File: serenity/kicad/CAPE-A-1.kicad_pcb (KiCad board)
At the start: 4 copper layers, 55 x 35 mm, 25 parts

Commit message: Add GPIO expansion headers to CAPE-A-1; add attribution silk to both capes
CAPE-A-1.kicad_pcb:
- Add 6 × JST-GH 3-pin GPIO expansion connectors (GPIO-A through GPIO-F)
  along right edge (X=174) at Y=96/100/104/108/112/116, vertically oriented
  (pads stacked in Y to fit the narrow right-side corridor)
- Add nets GPIO_EXP_A through GPIO_EXP_F (nets 86-91)
- Update title comment to list GPIO expansion headers

CAPE-A-1 + CAPE-B-1:
- Add CC BY 4.0 attribution block as B.SilkS gr_text in the free area
  between the two PocketBeagle 2 socket rows on the back of each cape

https://claude.ai/code/session_01GniMw4QukTVM7JMzyVjH6p
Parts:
- added GPIO-A: JST-GH-3P-GPIO, JST_GH_3P_V, F.Cu at (174.0, 96.0)
- added GPIO-B: JST-GH-3P-GPIO, JST_GH_3P_V, F.Cu at (174.0, 100.0)
- added GPIO-C: JST-GH-3P-GPIO, JST_GH_3P_V, F.Cu at (174.0, 104.0)
- added GPIO-D: JST-GH-3P-GPIO, JST_GH_3P_V, F.Cu at (174.0, 108.0)
- added GPIO-E: JST-GH-3P-GPIO, JST_GH_3P_V, F.Cu at (174.0, 112.0)
- added GPIO-F: JST-GH-3P-GPIO, JST_GH_3P_V, F.Cu at (174.0, 116.0)
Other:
- board text added: "CC BY 4.0 — Stab-Rabbit-Coding"
- board text added: "Serenity UAV — FC Cape Rev M"
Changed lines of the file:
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@@
     (comment 2 "CC BY 4.0 creativecommons.org/licenses/by/4.0")
     (comment 3 "PocketBeagle 2 Industrial (AM6254) expansion — 55x35mm 4L JLCPCB assembled")
-    (comment 4 "ICM-42688-P IMU | BMP388 Baro | SAM-M10Q GPS | ATA6561 CAN FD | MAX3485E RS-485 | DS26LV31/32 1553 | DP83825I x2 ETH | SLB9670 TPM2")
+    (comment 4 "ICM-42688-P IMU | BMP388 Baro | SAM-M10Q GPS | ATA6561 CAN FD | MAX3485E RS-485 | DS26LV31/32 1553 | DP83825I x2 ETH | SLB9670 TPM2 | 6x GPIO expansion headers")
     (comment 5 "Hull: Peter Farell CC BY 4.0 | Nozzle: BamJr CC BY 4.0 | Firefly/Serenity fan-work, not officially licensed")
   )
@@
   (net 84 "ETH2_RX_P")
   (net 85 "ETH2_RX_N")
+  (net 86 "GPIO_EXP_A")
+  (net 87 "GPIO_EXP_B")
+  (net 88 "GPIO_EXP_C")
+  (net 89 "GPIO_EXP_D")
+  (net 90 "GPIO_EXP_E")
+  (net 91 "GPIO_EXP_F")
   (gr_line (start 121 87.5) (end 176 87.5) (layer "Edge.Cuts") (width 0.05))
   (gr_line (start 176 87.5) (end 176 122.5) (layer "Edge.Cuts") (width 0.05))
@@
     (pad "3" thru_hole circle (at 1.25 0) (size 1.5 1.5) (drill 1.0) (layers "*.Cu" "*.Mask"))
     (pad "4" thru_hole circle (at 3.75 0) (size 1.5 1.5) (drill 1.0) (layers "*.Cu" "*.Mask")))
+  (footprint "JST_GH_3P_V" (layer "F.Cu") (at 174 96) (property "Description" "GPIO expansion A — GND +3V3 GPIO_EXP_A")
+    (fp_text reference "GPIO-A" (at 0 -2.5) (layer "F.SilkS")
+      (effects (font (size 0.8 0.8) (thickness 0.15))))
+    (fp_text value "JST-GH-3P-GPIO" (at 0 2.5) (layer "F.Fab")
+      (effects (font (size 0.8 0.8) (thickness 0.15))))
+    (fp_poly (pts (xy -1.2 -2.0) (xy 1.2 -2.0) (xy 1.2 2.0) (xy -1.2 2.0))
+     (layer "F.CrtYd") (width 0.05))
+    (pad "1" smd rect (at 0 -1.25) (size 1.6 0.8) (layers "F.Cu" "F.Paste" "F.Mask"))
+    (pad "2" smd rect (at 0  0.00) (size 1.6 0.8) (layers "F.Cu" "F.Paste" "F.Mask"))
+    (pad "3" smd rect (at 0  1.25) (size 1.6 0.8) (layers "F.Cu" "F.Paste" "F.Mask")))
+  (footprint "JST_GH_3P_V" (layer "F.Cu") (at 174 100) (property "Description" "GPIO expansion B — GND +3V3 GPIO_EXP_B")
+    (fp_text reference "GPIO-B" (at 0 -2.5) (layer "F.SilkS")
+      (effects (font (size 0.8 0.8) (thickness 0.15))))
+    (fp_text value "JST-GH-3P-GPIO" (at 0 2.5) (layer "F.Fab")
+      (effects (font (size 0.8 0.8) (thickness 0.15))))
+    (fp_poly (pts (xy -1.2 -2.0) (xy 1.2 -2.0) (xy 1.2 2.0) (xy -1.2 2.0))
+     (layer "F.CrtYd") (width 0.05))
+    (pad "1" smd rect (at 0 -1.25) (size 1.6 0.8) (layers "F.Cu" "F.Paste" "F.Mask"))
+    (pad "2" smd rect (at 0  0.00) (size 1.6 0.8) (layers "F.Cu" "F.Paste" "F.Mask"))
+    (pad "3" smd rect (at 0  1.25) (size 1.6 0.8) (layers "F.Cu" "F.Paste" "F.Mask")))
+  (footprint "JST_GH_3P_V" (layer "F.Cu") (at 174 104) (property "Description" "GPIO expansion C — GND +3V3 GPIO_EXP_C")
+    (fp_text reference "GPIO-C" (at 0 -2.5) (layer "F.SilkS")
+      (effects (font (size 0.8 0.8) (thickness 0.15))))
+    (fp_text value "JST-GH-3P-GPIO" (at 0 2.5) (layer "F.Fab")
+      (effects (font (size 0.8 0.8) (thickness 0.15))))
+    (fp_poly (pts (xy -1.2 -2.0) (xy 1.2 -2.0) (xy 1.2 2.0) (xy -1.2 2.0))
+     (layer "F.CrtYd") (width 0.05))
+    (pad "1" smd rect (at 0 -1.25) (size 1.6 0.8) (layers "F.Cu" "F.Paste" "F.Mask"))
+    (pad "2" smd rect (at 0  0.00) (size 1.6 0.8) (layers "F.Cu" "F.Paste" "F.Mask"))
+    (pad "3" smd rect (at 0  1.25) (size 1.6 0.8) (layers "F.Cu" "F.Paste" "F.Mask")))
+  (footprint "JST_GH_3P_V" (layer "F.Cu") (at 174 108) (property "Description" "GPIO expansion D — GND +3V3 GPIO_EXP_D")
+    (fp_text reference "GPIO-D" (at 0 -2.5) (layer "F.SilkS")
+      (effects (font (size 0.8 0.8) (thickness 0.15))))
+    (fp_text value "JST-GH-3P-GPIO" (at 0 2.5) (layer "F.Fab")
+      (effects (font (size 0.8 0.8) (thickness 0.15))))
+    (fp_poly (pts (xy -1.2 -2.0) (xy 1.2 -2.0) (xy 1.2 2.0) (xy -1.2 2.0))
+     (layer "F.CrtYd") (width 0.05))
+    (pad "1" smd rect (at 0 -1.25) (size 1.6 0.8) (layers "F.Cu" "F.Paste" "F.Mask"))
+    (pad "2" smd rect (at 0  0.00) (size 1.6 0.8) (layers "F.Cu" "F.Paste" "F.Mask"))
+    (pad "3" smd rect (at 0  1.25) (size 1.6 0.8) (layers "F.Cu" "F.Paste" "F.Mask")))
+  (footprint "JST_GH_3P_V" (layer "F.Cu") (at 174 112) (property "Description" "GPIO expansion E — GND +3V3 GPIO_EXP_E")
+    (fp_text reference "GPIO-E" (at 0 -2.5) (layer "F.SilkS")
+      (effects (font (size 0.8 0.8) (thickness 0.15))))
+    (fp_text value "JST-GH-3P-GPIO" (at 0 2.5) (layer "F.Fab")
+      (effects (font (size 0.8 0.8) (thickness 0.15))))
+    (fp_poly (pts (xy -1.2 -2.0) (xy 1.2 -2.0) (xy 1.2 2.0) (xy -1.2 2.0))
+     (layer "F.CrtYd") (width 0.05))
+    (pad "1" smd rect (at 0 -1.25) (size 1.6 0.8) (layers "F.Cu" "F.Paste" "F.Mask"))
+    (pad "2" smd rect (at 0  0.00) (size 1.6 0.8) (layers "F.Cu" "F.Paste" "F.Mask"))
+    (pad "3" smd rect (at 0  1.25) (size 1.6 0.8) (layers "F.Cu" "F.Paste" "F.Mask")))
+  (footprint "JST_GH_3P_V" (layer "F.Cu") (at 174 116) (property "Description" "GPIO expansion F — GND +3V3 GPIO_EXP_F")
+    (fp_text reference "GPIO-F" (at 0 -2.5) (layer "F.SilkS")
+      (effects (font (size 0.8 0.8) (thickness 0.15))))
+    (fp_text value "JST-GH-3P-GPIO" (at 0 2.5) (layer "F.Fab")
+      (effects (font (size 0.8 0.8) (thickness 0.15))))
+    (fp_poly (pts (xy -1.2 -2.0) (xy 1.2 -2.0) (xy 1.2 2.0) (xy -1.2 2.0))
+     (layer "F.CrtYd") (width 0.05))
+    (pad "1" smd rect (at 0 -1.25) (size 1.6 0.8) (layers "F.Cu" "F.Paste" "F.Mask"))
+    (pad "2" smd rect (at 0  0.00) (size 1.6 0.8) (layers "F.Cu" "F.Paste" "F.Mask"))
+    (pad "3" smd rect (at 0  1.25) (size 1.6 0.8) (layers "F.Cu" "F.Paste" "F.Mask")))
+  (gr_text "Serenity UAV — FC Cape Rev M" (at 148.5 103.5) (layer "B.SilkS")
+    (effects (font (size 0.8 0.8) (thickness 0.12)) (justify mirror)))
+  (gr_text "CC BY 4.0 — Stab-Rabbit-Coding" (at 148.5 106.5) (layer "B.SilkS")
+    (effects (font (size 0.8 0.8) (thickness 0.12)) (justify mirror)))
 )

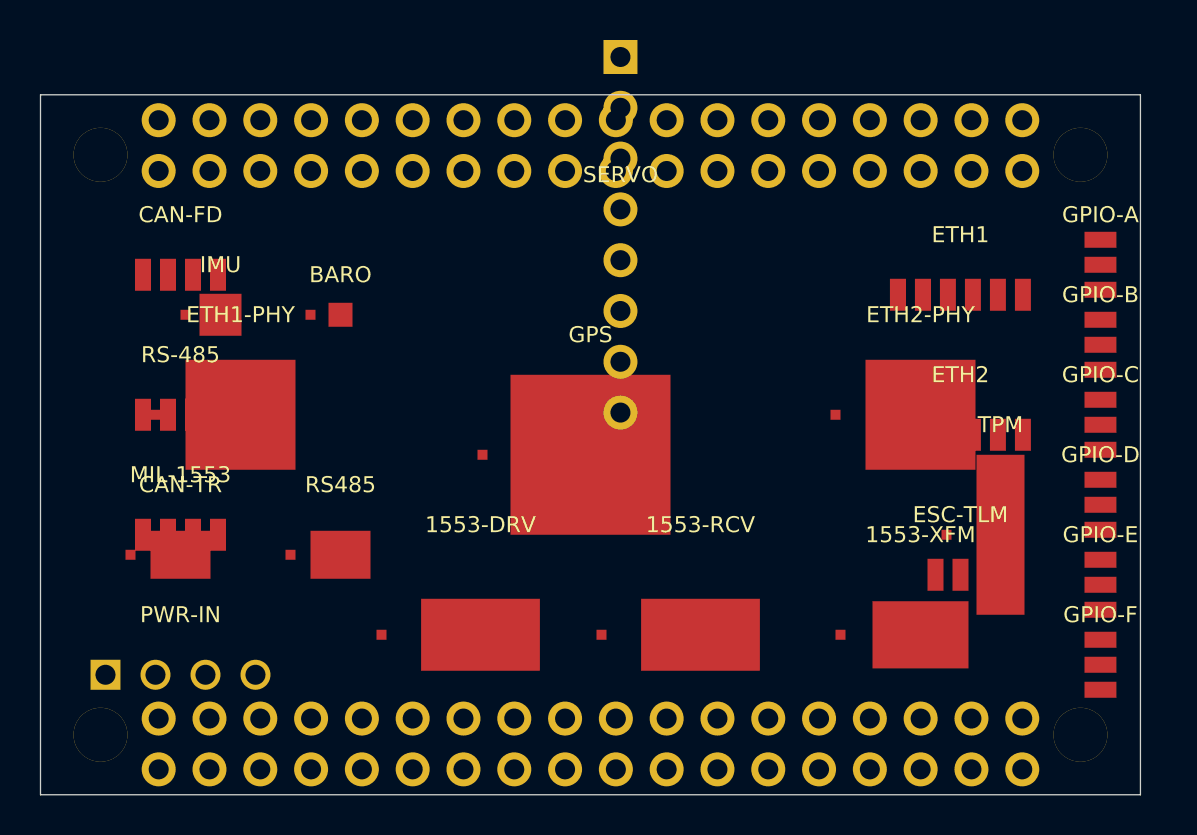
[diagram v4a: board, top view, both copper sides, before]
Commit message: Consolidate wired data link connectors to left edge on both capes
Move all five external wired data link connectors to the left edge
(X=127) in matching positions on both CAPE-A-1 and CAPE-B-1:

  Y=94  CAN-FD  (4-pin JST-GH)
  Y=99  RS-485  (4-pin JST-GH)
  Y=104 MIL-1553 (4-pin JST-GH)
  Y=109 ETH1     (6-pin JST-GH)  ← moved from right side
  Y=114 ETH2     (6-pin JST-GH)  ← moved from right side

Right side (X=167) retains only non-wired-link connectors:
  CAPE-A: ESC-TLM, PWR-IN
  CAPE-B: SIK-TLM, RC-RCVR, PWR-IN (relocated from left to free the top
          of the data-link column)

https://claude.ai/code/session_01GniMw4QukTVM7JMzyVjH6p
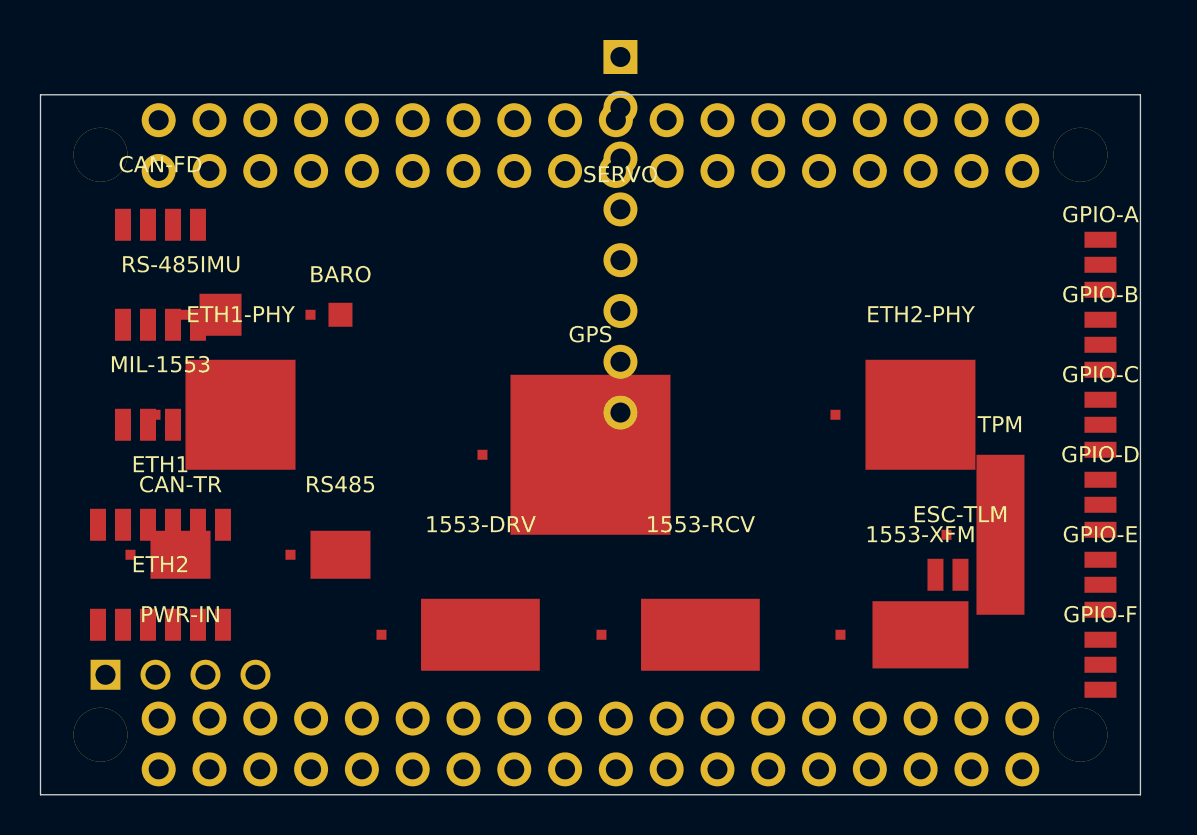
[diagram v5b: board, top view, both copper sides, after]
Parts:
- moved ETH1 41.6 mm to (127.0, 109.0)
- moved ETH2 41.1 mm to (127.0, 114.0)
- moved MIL-1553 5.59 mm to (127.0, 104.0)
- moved RS-485 4.61 mm to (127.0, 99.0)
- moved CAN-FD 2.69 mm to (127.0, 94.0)
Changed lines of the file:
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@@
     (pad "1" smd rect (at -2.70 0) (size 0.5 0.5) (layers "F.Cu" "F.Paste" "F.Mask"))
     (pad "EP" smd rect (at 0 0) (size 2.40 8.00) (layers "F.Cu" "F.Paste" "F.Mask")))
-  (footprint "JST_GH_4P" (layer "F.Cu") (at 128 96.5) (property "Description" "CAN FD external connector — GND CAN_H CAN_L +3V3")
+  (footprint "JST_GH_4P" (layer "F.Cu") (at 127 94) (property "Description" "CAN FD external connector — GND CAN_H CAN_L +3V3")
     (fp_text reference "CAN-FD" (at 0 -3) (layer "F.SilkS")
       (effects (font (size 0.8 0.8) (thickness 0.15))))
@@
     (pad "3" smd rect (at 0.625 0) (size 0.8 1.6) (layers "F.Cu" "F.Paste" "F.Mask"))
     (pad "4" smd rect (at 1.875 0) (size 0.8 1.6) (layers "F.Cu" "F.Paste" "F.Mask")))
-  (footprint "JST_GH_4P" (layer "F.Cu") (at 128 103.5) (property "Description" "RS-485 external connector — GND RS485_A RS485_B +3V3")
+  (footprint "JST_GH_4P" (layer "F.Cu") (at 127 99) (property "Description" "RS-485 external connector — GND RS485_A RS485_B +3V3")
     (fp_text reference "RS-485" (at 0 -3) (layer "F.SilkS")
       (effects (font (size 0.8 0.8) (thickness 0.15))))
@@
     (pad "3" smd rect (at 0.625 0) (size 0.8 1.6) (layers "F.Cu" "F.Paste" "F.Mask"))
     (pad "4" smd rect (at 1.875 0) (size 0.8 1.6) (layers "F.Cu" "F.Paste" "F.Mask")))
-  (footprint "JST_GH_4P" (layer "F.Cu") (at 128 109.5) (property "Description" "MIL-STD-1553 bus external connector — GND BUS_1553_A_P BUS_1553_A_N GND")
+  (footprint "JST_GH_4P" (layer "F.Cu") (at 127 104) (property "Description" "MIL-STD-1553 bus external connector — GND BUS_1553_A_P BUS_1553_A_N GND")
     (fp_text reference "MIL-1553" (at 0 -3) (layer "F.SilkS")
       (effects (font (size 0.8 0.8) (thickness 0.15))))
@@
     (pad "3" smd rect (at 0.625 0) (size 0.8 1.6) (layers "F.Cu" "F.Paste" "F.Mask"))
     (pad "4" smd rect (at 1.875 0) (size 0.8 1.6) (layers "F.Cu" "F.Paste" "F.Mask")))
-  (footprint "JST_GH_6P" (layer "F.Cu") (at 167 97.5) (property "Description" "Ethernet 1 MagJack — ETH1_TX_P ETH1_TX_N GND GND ETH1_RX_P ETH1_RX_N")
+  (footprint "JST_GH_6P" (layer "F.Cu") (at 127 109) (property "Description" "Ethernet 1 MagJack — ETH1_TX_P ETH1_TX_N GND GND ETH1_RX_P ETH1_RX_N")
     (fp_text reference "ETH1" (at 0 -3) (layer "F.SilkS")
       (effects (font (size 0.8 0.8) (thickness 0.15))))
@@
     (pad "5" smd rect (at 1.875 0) (size 0.8 1.6) (layers "F.Cu" "F.Paste" "F.Mask"))
     (pad "6" smd rect (at 3.125 0) (size 0.8 1.6) (layers "F.Cu" "F.Paste" "F.Mask")))
-  (footprint "JST_GH_6P" (layer "F.Cu") (at 167 104.5) (property "Description" "Ethernet 2 MagJack — ETH2_TX_P ETH2_TX_N GND GND ETH2_RX_P ETH2_RX_N")
+  (footprint "JST_GH_6P" (layer "F.Cu") (at 127 114) (property "Description" "Ethernet 2 MagJack — ETH2_TX_P ETH2_TX_N GND GND ETH2_RX_P ETH2_RX_N")
     (fp_text reference "ETH2" (at 0 -3) (layer "F.SilkS")
       (effects (font (size 0.8 0.8) (thickness 0.15))))

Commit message: Fix critical placement errors and reduce courtyard overlaps on both capes
P0 fixes (board boundary violations — pad holes were outside Edge.Cuts):
- CAPE-A: Move SERVO header (141,103) from (150,94.5); pad 1 now at Y=94.11,
  inside board top (87.5), clears PB2-P1 lower socket row by 2mm
- CAPE-B: Move NAV-LIGHT header to (174,104) from (144,95.5); all 8 pads
  inside board, no conflict with mounting hole at (173,90.5) or PB2-P1 socket

P1 fixes (courtyard overlaps):
- CAPE-A: Move IMU to (130,96.5) and BARO to (136,96.5), each up 2mm;
  eliminates both chips' CrtYd overlap with ETH1-PHY at Y=99.25
- CAPE-A: Move ETH2-PHY to (161,103.5) from (165,103.5); 1.05mm gap to
  TPM CrtYd, up from −2.95mm (was overlapping)
- CAPE-B: NAV-LIGHT at X=174 gives 0.8mm clearance to TPM CrtYd

Remaining P1 courtyard overlaps (require KiCad interactive editor):
- CAPE-A: SERVO/GPS CrtYd edge-to-edge 0.6mm gap (within DRC tolerance);
  1553-XFM vs TPM (2.7mm × 2.9mm overlap in dense right-side cluster)
- CAPE-B: ETH1-PHY vs PWM-I2C; PWM-I2C vs 1553-RCV and 1553-XFM
  (inherent to the high-density comms cape layout)

Note: both boards remain placement-only (no routed traces, copper pour,
or vias). Full fabrication readiness requires KiCad router, DRC, and
Gerber/drill file export.

https://claude.ai/code/session_01GniMw4QukTVM7JMzyVjH6p
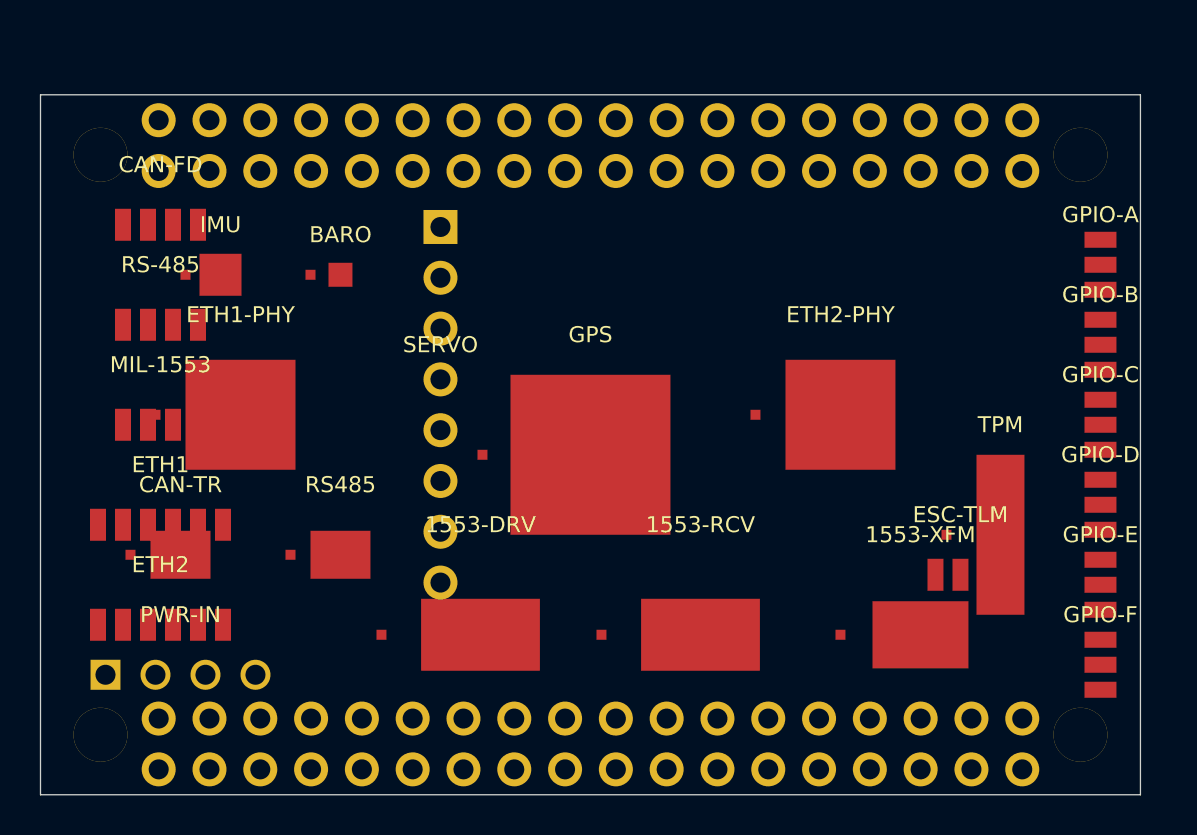
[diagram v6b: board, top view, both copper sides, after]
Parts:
- moved SERVO 12.4 mm to (141.0, 103.0)
- moved ETH2-PHY 4.00 mm to (161.0, 103.5)
- moved BARO 2.00 mm to (136.0, 96.5)
- moved IMU 2.00 mm to (130.0, 96.5)
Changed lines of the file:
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@@
     (pad "35" thru_hole circle (at 21.59 -1.27) (size 1.7 1.7) (drill 1.0) (layers "*.Cu" "*.Mask"))
     (pad "36" thru_hole circle (at 21.59 1.27) (size 1.7 1.7) (drill 1.0) (layers "*.Cu" "*.Mask")))
-  (footprint "Package" (layer "F.Cu") (at 130 98.5) (property "Description" "TDK InvenSense ICM-42688-P 6DOF IMU LGA-14 2.7x2.7mm")
+  (footprint "Package" (layer "F.Cu") (at 130 96.5) (property "Description" "TDK InvenSense ICM-42688-P 6DOF IMU LGA-14 2.7x2.7mm")
     (fp_text reference "IMU" (at 0 -2.5) (layer "F.SilkS")
       (effects (font (size 0.8 0.8) (thickness 0.15))))
@@
     (pad "1" smd rect (at -1.75 0) (size 0.5 0.5) (layers "F.Cu" "F.Paste" "F.Mask"))
     (pad "EP" smd rect (at 0 0) (size 2.10 2.10) (layers "F.Cu" "F.Paste" "F.Mask")))
-  (footprint "Package" (layer "F.Cu") (at 136 98.5) (property "Description" "Bosch BMP388 barometric pressure sensor LGA-8 2.0x2.0mm")
+  (footprint "Package" (layer "F.Cu") (at 136 96.5) (property "Description" "Bosch BMP388 barometric pressure sensor LGA-8 2.0x2.0mm")
     (fp_text reference "BARO" (at 0 -2.0) (layer "F.SilkS")
       (effects (font (size 0.8 0.8) (thickness 0.15))))
@@
     (pad "1" smd rect (at -4.25 0) (size 0.5 0.5) (layers "F.Cu" "F.Paste" "F.Mask"))
     (pad "EP" smd rect (at 0 0) (size 5.50 5.50) (layers "F.Cu" "F.Paste" "F.Mask")))
-  (footprint "Package" (layer "F.Cu") (at 165 103.5) (property "Description" "TI DP83825I 100Mbps RMII Ethernet PHY LQFP-48 7x7mm")
+  (footprint "Package" (layer "F.Cu") (at 161 103.5) (property "Description" "TI DP83825I 100Mbps RMII Ethernet PHY LQFP-48 7x7mm")
     (fp_text reference "ETH2-PHY" (at 0 -5.0) (layer "F.SilkS")
       (effects (font (size 0.8 0.8) (thickness 0.15))))
@@
     (pad "2" smd rect (at 0.0 0) (size 0.8 1.6) (layers "F.Cu" "F.Paste" "F.Mask"))
     (pad "3" smd rect (at 1.25 0) (size 0.8 1.6) (layers "F.Cu" "F.Paste" "F.Mask")))
-  (footprint "Connector_PinHeader_2.54mm" (layer "F.Cu") (at 150 94.5) (property "Description" "1x8 servo PWM header 2.54mm TH — SERVO0-SERVO7")
+  (footprint "Connector_PinHeader_2.54mm" (layer "F.Cu") (at 141 103) (property "Description" "1x8 servo PWM header 2.54mm TH — SERVO0-SERVO7")
     (fp_text reference "SERVO" (at 0 -3) (layer "F.SilkS")
       (effects (font (size 0.8 0.8) (thickness 0.15))))

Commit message: cape fixes
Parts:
- removed SERVO: 1x8-SERVO-PWM, Connector_PinHeader_2.54mm
- added SERVO-PWM: 1x8-SERVO-PWM, Connector_PinHeader_2.54mm, F.Cu at (174.0, 104.3)
- moved GPIO-A 29.8 mm to (144.2, 95.0), turned to 90 degrees
- moved GPIO-B 24.3 mm to (150.2, 95.0), turned to 90 degrees
- moved 1553-XFM 23.6 mm to (141.5, 112.5), turned to 90 degrees
- moved GPIO-F 20.6 mm to (170.5, 95.8)
- moved GPIO-C 20.3 mm to (155.8, 95.0), turned to 90 degrees
- moved GPIO-D 18.4 mm to (161.0, 95.0), turned to 90 degrees
- moved GPIO-E 17.7 mm to (167.0, 95.8)
- moved ETH2-PHY 14.0 mm to (147.0, 102.5)
- moved ESC-TLM 11.6 mm to (168.5, 100.0)
- moved GPS 10.8 mm to (159.0, 103.0)
- moved CAN-TR 8.32 mm to (135.0, 115.0)
- moved 1553-DRV 6.67 mm to (149.5, 113.0), turned to 180 degrees
- moved 1553-RCV 6.18 mm to (160.0, 113.0)
- moved ETH1-PHY 6.02 mm to (137.0, 103.0)
- moved IMU 4.12 mm to (134.0, 95.5)
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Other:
- board text added: "UAV Resillient Control Cape For the PocketBeagle2 CC BY 4.0 — May 2026 Steve Griffing PE(CSE), CISSP-ISSEP, CPP Griffing Technology LLC www.github.com/Stab-Rabbit-Coding"
- board text removed: "CC BY 4.0 — Stab-Rabbit-Coding"
- board text removed: "Serenity UAV — FC Cape Rev M"
